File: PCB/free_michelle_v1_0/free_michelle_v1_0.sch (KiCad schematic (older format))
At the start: 28 parts

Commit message: Poprawione zapomniane polaczenie led WS do uC
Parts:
- removed J?: WS2812b, symbol Connector:Conn_01x03_Male
- added J?: WS2812b, symbol Connector:Conn_01x04_Male
- added J?: DS18B20, symbol Connector:Conn_01x04_Male
- U?: symbol free_michelle_v1_0-cache:grad73_library_24AA01 -> free_michelle_v1_0-rescue:grad73_library_24AA01-free_michelle_v1_0-cache
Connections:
- net labels added: DS18B20_1WIRE_PA15
- wire segments 203 -> 210
- no-connect marks 6 -> 8
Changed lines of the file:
@@
 $EndComp
 $Comp
-L free_michelle_v1_0-cache:grad73_library_24AA01 U?
+L free_michelle_v1_0-rescue:grad73_library_24AA01-free_michelle_v1_0-cache U?
 U 1 1 61E51F54
 P 2140 7830
@@
 NoConn ~ 9300 6090
 NoConn ~ 9300 6190
-$Comp
-L Connector:Conn_01x03_Male J?
-U 1 1 61FEF438
-P 12700 6000
-F 0 "J?" H 12808 6281 50  0000 C CNN
-F 1 "WS2812b" H 12808 6190 50  0000 C CNN
-F 2 "" H 12700 6000 50  0001 C CNN
-F 3 "~" H 12700 6000 50  0001 C CNN
-	1    12700 6000
-	-1   0    0    1
-$EndComp
 $Comp
 L power:+5VP #PWR?
@@
 Wire Wire Line
 	11900 5600 11900 6000
+$Comp
+L Connector:Conn_01x04_Male J?
+U 1 1 622B6E8C
+P 12700 6100
+F 0 "J?" H 12672 5982 50  0000 R CNN
+F 1 "WS2812b" H 12672 6073 50  0000 R CNN
+F 2 "" H 12700 6100 50  0001 C CNN
+F 3 "~" H 12700 6100 50  0001 C CNN
+	1    12700 6100
+	-1   0    0    1
+$EndComp
+NoConn ~ 12500 6200
+$Comp
+L Connector:Conn_01x04_Male J?
+U 1 1 622CF0D8
+P 14660 6100
+F 0 "J?" H 14632 5982 50  0000 R CNN
+F 1 "DS18B20" H 14632 6073 50  0000 R CNN
+F 2 "" H 14660 6100 50  0001 C CNN
+F 3 "~" H 14660 6100 50  0001 C CNN
+	1    14660 6100
+	-1   0    0    1
+$EndComp
+$Comp
+L power:+5V #PWR?
+U 1 1 622CFE05
+P 14300 5800
+F 0 "#PWR?" H 14300 5650 50  0001 C CNN
+F 1 "+5V" H 14315 5973 50  0000 C CNN
+F 2 "" H 14300 5800 50  0001 C CNN
+F 3 "" H 14300 5800 50  0001 C CNN
+	1    14300 5800
+	1    0    0    -1
+$EndComp
+Wire Wire Line
+	14460 5900 14300 5900
+Wire Wire Line
+	14300 5900 14300 5800
+$Comp
+L power:GND #PWR?
+U 1 1 622DBDAF
+P 14300 6300
+F 0 "#PWR?" H 14300 6050 50  0001 C CNN
+F 1 "GND" H 14305 6127 50  0000 C CNN
+F 2 "" H 14300 6300 50  0001 C CNN
+F 3 "" H 14300 6300 50  0001 C CNN
+	1    14300 6300
+	1    0    0    -1
+$EndComp
+Wire Wire Line
+	14300 6300 14300 6100
+Wire Wire Line
+	14300 6100 14460 6100
+Text GLabel 14100 6000 0    39   Input ~ 0
+DS18B20_1WIRE_PA15
+Wire Wire Line
+	14460 6000 14100 6000
+NoConn ~ 14460 6200
+Wire Wire Line
+	9340 2260 8600 2260
+Text GLabel 8600 2260 0    39   Input ~ 0
+WS2812b_PA9
+Text GLabel 8590 2660 0    39   Input ~ 0
+DS18B20_1WIRE_PA15
+Wire Wire Line
+	8590 2660 9340 2660
 $EndSCHEMATC

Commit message: Dodane przekazniki z tranzystorami kluczującymi
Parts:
- added D? (x8): 1N4148, symbol Device:D_Small_ALT
- added J? (x8): ARK, symbol Connector:Conn_01x03_Female
- added K? (x8): FINDER-36.11, Relay_THT:Relay_SPDT_Finder_36.11, symbol Relay:FINDER-36.11
- added Q? (x8): MMBT4403_PNP, Package_TO_SOT_SMD:SOT-23, symbol Transistor_BJT:MMBT3906
- added R? (x8): 2.2k, symbol Device:R_Small
- added R? (x8): 10k, symbol Device:R_Small
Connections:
- net +3V3: now also Q?.2 (E), Q?.2 (E), Q?.2 (E), Q?.2 (E), Q?.2 (E), Q?.2 (E), Q?.2 (E), Q?.2 (E)
- net GND: now also R?.1, R?.1, R?.1, R?.1, R?.1, R?.1, R?.1, R?.1
- net RELAY4_PB12: now reaches GPIO_CONTROLLER.21 (PB12)
- net RELAY4_PB12: now also R?.1
- net RELAY3_PB13: now reaches GPIO_CONTROLLER.22 (PB13)
- net RELAY3_PB13: now also R?.1
- net RELAY2_PB14: now reaches GPIO_CONTROLLER.23 (PB14)
- net RELAY2_PB14: now also R?.1
- net RELAY1_PB15: now reaches GPIO_CONTROLLER.24 (PB15)
- net RELAY1_PB15: now also R?.1
- net LIGHT4_PB4: now reaches GPIO_CONTROLLER.32 (PB4)
- net LIGHT4_PB4: now also R?.1
- net LIGHT3_PB5: now reaches GPIO_CONTROLLER.33 (PB5)
- net LIGHT3_PB5: now also R?.1
- net LIGHT2_PB6: now reaches GPIO_CONTROLLER.34 (PB6)
- net LIGHT2_PB6: now also R?.1
- net LIGHT1_PB7: now reaches GPIO_CONTROLLER.35 (PB7)
- net LIGHT1_PB7: now also R?.1
- new net: Q?.1 (B), R?.2 (x8)
- new net: D?.1 (K), K?.A1, Q?.3 (C) (x8)
- new net: J?.2 (Pin_2), K?.11 (x8)
- new net: J?.1 (Pin_1), K?.12 (x8)
- new net: J?.3 (Pin_3), K?.14 (x8)
- new net: D?.2 (A), K?.A2, R?.2 (x8)
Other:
- moved on the sheet: C1, C?, CR2032, D?, J?, Q?, R1, R2, R3, R4, R5, R?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

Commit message: Dodao i podlaczona nRF24
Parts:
- added C?: 1uF, symbol Device:C_Small
- added U?: ESP-12E, RF_Module:ESP-12E, symbol RF_Module:ESP-12E
- added U?: NRF24L01_Breakout, RF_Module:nRF24L01_Breakout, symbol RF:NRF24L01_Breakout
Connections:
- net labels added: nRF24_CE_PB1, nRF24_CSN_PA11, nRF24_IRQ_PB2, nRF24_MISO_PA12, nRF24_MOSI_PA10, nRF24_SCK_PB0
- wire segments 418 -> 440
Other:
- moved on the sheet: R4, R5, U?

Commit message: Dodane opisy i podział bloków na schemacie
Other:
- note added: "MIKROKONTROLER DO STEROWANIA GPIO I CZUJNIKAMI"
- note added: "MIKROKONTROLER DO STEROWANIA MENU I TFT"
- note added: "PRZEKAŹNIKI"
- note added: "ZASILANIE"
- note added: "ŁĄCZNOŚĆ BEZPRZEWODOWA"
- moved on the sheet: C1, C?, CR2032, D?, GPIO_CONTROLLER, J?, K?, Q?, R1, R2, R3, R4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

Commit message: Dosane ESP do schematu
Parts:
- removed U?: ESP-12E, RF_Module:ESP-12E, symbol RF_Module:ESP-12E
- added J?: Zworka_RX, symbol Connector:Conn_01x02_Male
- added J?: Zworka_TX, symbol Connector:Conn_01x02_Male
- added U?: ESP8266_NodeMCU_v2, symbol grad73_library:ESP8266_NodeMCU_v2
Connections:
- net labels added: DS3231_SCL_I2C3_PA8, DS3231_SDA_I2C3_PB8, ESP_RX_TX_STM__U1_PA15, ESP_TX_RX_STM__U1_PB7
- wire segments 440 -> 455
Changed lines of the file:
@@
 NoConn ~ 5830 6500
 Text GLabel 4490 6500 0    39   Input ~ 0
-DS3231_SCL_PB6
+DS3231_SCL_I2C3_PA8
 Text GLabel 2840 3360 0    39   Input ~ 0
 DS3231_SCL_PB6
@@
 	2840 3360 2990 3360
 Text GLabel 4490 6600 0    39   Input ~ 0
-DS3231_SDA_PB7
+DS3231_SDA_I2C3_PB8
 Text GLabel 2840 3460 0    39   Input ~ 0
 DS3231_SDA_PB7
@@
 Wire Wire Line
 	9780 3320 10580 3320
-$Comp
-L RF_Module:ESP-12E U?
-U 1 1 6282E130
-P 2970 11730
-F 0 "U?" H 2970 12711 50  0000 C CNN
-F 1 "ESP-12E" H 2970 12620 50  0000 C CNN
-F 2 "RF_Module:ESP-12E" H 2970 11730 50  0001 C CNN
-F 3 "http://wiki.ai-thinker.com/_media/esp8266/esp8266_series_modules_user_manual_v1.1.pdf" H 2620 11830 50  0001 C CNN
-	1    2970 11730
-	1    0    0    -1
-$EndComp
-$Comp
-L power:GND #PWR?
-U 1 1 62831A59
-P 2970 12590
-F 0 "#PWR?" H 2970 12340 50  0001 C CNN
-F 1 "GND" H 2975 12417 50  0000 C CNN
-F 2 "" H 2970 12590 50  0001 C CNN
-F 3 "" H 2970 12590 50  0001 C CNN
-	1    2970 12590
-	1    0    0    -1
-$EndComp
-Wire Wire Line
-	2970 12590 2970 12430
-$Comp
-L power:+3.3V #PWR?
-U 1 1 6285E1BD
-P 2970 10650
-F 0 "#PWR?" H 2970 10500 50  0001 C CNN
-F 1 "+3.3V" H 2985 10823 50  0000 C CNN
-F 2 "" H 2970 10650 50  0001 C CNN
-F 3 "" H 2970 10650 50  0001 C CNN
-	1    2970 10650
-	1    0    0    -1
-$EndComp
-Wire Wire Line
-	2970 10930 2970 10650
 $Comp
 L RF:NRF24L01_Breakout U?
@@
 Text Notes 18490 1270 0    118  ~ 0
 ZASILANIE
+$Comp
+L grad73_library:ESP8266_NodeMCU_v2 U?
+U 1 1 6342D07E
+P 2860 10460
+F 0 "U?" H 2860 10528 118 0000 C CNN
+F 1 "ESP8266_NodeMCU_v2" H 2860 10335 118 0000 C CNN
+F 2 "" H 3210 10460 118 0001 C CNN
+F 3 "" H 3210 10460 118 0001 C CNN
+	1    2860 10460
+	1    0    0    -1
+$EndComp
+$Comp
+L Connector:Conn_01x02_Male J?
+U 1 1 634309E9
+P 3670 11760
+F 0 "J?" V 3732 11804 50  0000 L CNN
+F 1 "Zworka_RX" V 3823 11804 50  0000 L CNN
+F 2 "" H 3670 11760 50  0001 C CNN
+F 3 "~" H 3670 11760 50  0001 C CNN
+	1    3670 11760
+	0    1    1    0
+$EndComp
+Wire Wire Line
+	3570 11960 3410 11960
+$Comp
+L Connector:Conn_01x02_Male J?
+U 1 1 63464817
+P 3570 12260
+F 0 "J?" V 3724 12072 50  0000 R CNN
+F 1 "Zworka_TX" V 3633 12072 50  0000 R CNN
+F 2 "" H 3570 12260 50  0001 C CNN
+F 3 "~" H 3570 12260 50  0001 C CNN
+	1    3570 12260
+	0    -1   -1   0
+$EndComp
+Wire Wire Line
+	3570 12060 3410 12060
+$Comp
+L power:GND #PWR?
+U 1 1 634CC58F
+P 3470 12600
+F 0 "#PWR?" H 3470 12350 50  0001 C CNN
+F 1 "GND" H 3475 12427 50  0000 C CNN
+F 2 "" H 3470 12600 50  0001 C CNN
+F 3 "" H 3470 12600 50  0001 C CNN
+	1    3470 12600
+	1    0    0    -1
+$EndComp
+Wire Wire Line
+	3410 12160 3470 12160
+Wire Wire Line
+	3470 12160 3470 12510
+Wire Wire Line
+	2310 11760 2170 11760
+Wire Wire Line
+	2170 11760 2170 12160
+Wire Wire Line
+	2170 12510 3470 12510
+Wire Wire Line
+	3470 12510 3470 12600
+Connection ~ 3470 12510
+Wire Wire Line
+	2310 12160 2170 12160
+Connection ~ 2170 12160
+Wire Wire Line
+	2170 12160 2170 12510
+$Comp
+L power:+5V #PWR?
+U 1 1 63605998
+P 1870 12110
+F 0 "#PWR?" H 1870 11960 50  0001 C CNN
+F 1 "+5V" H 1885 12283 50  0000 C CNN
+F 2 "" H 1870 12110 50  0001 C CNN
+F 3 "" H 1870 12110 50  0001 C CNN
+	1    1870 12110
+	1    0    0    -1
+$EndComp
+Wire Wire Line
+	2310 12260 1870 12260
+Wire Wire Line
+	1870 12260 1870 12110
+Text GLabel 4280 11960 2    39   Input ~ 0
+ESP_RX_TX_STM__U1_PA15
+Wire Wire Line
+	3410 11460 4200 11460
+Wire Wire Line
+	4200 11460 4200 12510
+Wire Wire Line
+	4200 12510 3480 12510
+Wire Wire Line
+	4280 11960 3670 11960
+Text GLabel 4280 12060 2    39   Input ~ 0
+ESP_TX_RX_STM__U1_PB7
+Wire Wire Line
+	3670 12060 4280 12060
 $EndSCHEMATC

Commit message: Dosane przelaczniki wlaczania zasilania i zlacza do schematu
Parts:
- added C?: 47uF, symbol Device:CP_Small
- added C? (x2): 100nF, symbol Device:C_Small
- added D?: GREEN_USER_LED, symbol Device:LED
- added D?: RED_LED, symbol Device:LED
- added D?: YELLOW_LED, symbol Device:LED
- added J?: A02YYUW_GroveCON, symbol Connector:Conn_01x04_Male
- added J?: Gniazdo 9V DC 5,5x2,5, symbol Connector:Conn_01x02_Male
- added J?: Gniazdo 5VP DC 5,5x2,5, symbol Connector:Conn_01x02_Male
- added R?: 110, symbol Device:R_Small
- added R?: 730, symbol Device:R_Small
- added R?: 290, symbol Device:R_Small
- added SW?: Rotary_Encoder_Switch, symbol Device:Rotary_Encoder_Switch
- added SW? (x2): SW_Push, symbol Switch:SW_Push
- added U?: LD1117V33, symbol grad73_library:LD1117V33
- J? (x2): value SW -> GROVE_SW
- J?: value WS2812b -> WS2812b_GroveCON
- J?: value DS18B20 -> DS18B20_GroveCON
- U?: value DS3231M -> DS3231M_RTC
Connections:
- net DS3231_SCL_I2C3_PA8 is gone; now on net DS3231_SCL_PB6: R2.1, R3.1, U?.16 (SCL)
- net DS3231_SDA_I2C3_PB8 is gone; now on net DS3231_SDA_PB9: U?.15 (SDA)
- net DS3231_SDA_PB7 is gone; now on net ESP_TX_RX_STM__U1_PB7: TFT_CONTROLLER.35 (PB7)
- net +3V3: no longer Q?.2 (E), Q?.2 (E), Q?.2 (E), Q?.2 (E), Q?.2 (E), Q?.2 (E), Q?.2 (E), Q?.2 (E)
- net +5V: now also J?.2 (Pin_2), J?.4 (Pin_4), SW?.A
- net +5VP: now also R?.1
- net +9V: now also C?.1, C?.1, R?.1, U?.1 (IN)
- net ESP_RX_TX_STM__U1_PA15: now also TFT_CONTROLLER.30 (PA15)
- net ESP_TX_RX_STM__U1_PB7: no longer J?.2 (Pin_2)
- net GND: now also C?.2, C?.2, C?.2, J?.1 (Pin_1), J?.1 (Pin_1), J?.3 (Pin_3), R?.1, SW?.B, U?.2 (GND)
- net DS3231_SDA_PB9: now reaches TFT_CONTROLLER.37 (PB9)
- net ENC_DT_PA0: now reaches TFT_CONTROLLER.6 (PA0)
- net ENC_DT_PA0: now also SW?.S1
- net ENC_CLK_PA1: now reaches TFT_CONTROLLER.7 (PA1)
- net ENC_CLK_PA1: now also SW?.S2
- net USER_LED_PA10: now reaches GPIO_CONTROLLER.27 (PA10)
- net USER_LED_PA10: now also D?.2 (A)
- net A02YYUW_U6_RX_PA12: now reaches GPIO_CONTROLLER.29 (PA12)
- net A02YYUW_U6_RX_PA12: now also J?.1 (Pin_1)
- new net: D?.1 (K), R?.2 (x3)
- new net: J?.2 (Pin_2), SW?.2 (x2)
- new net: D?.2 (A), SW?.1 (x2)
- new net +3.3VP: C?.1, Q?.2 (E), Q?.2 (E), Q?.2 (E), Q?.2 (E), Q?.2 (E), Q?.2 (E), Q?.2 (E), Q?.2 (E), U?.3 (OUT)
- no-connect marks 8 -> 59
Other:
- note added: "NAPIĘCIE ZASILANIA 3,3V"
- note added: "NAPIĘCIE ZASILANIA 5V"
- moved on the sheet: C?, D?, J?, K?, Q?, R4, R5, R?, U?

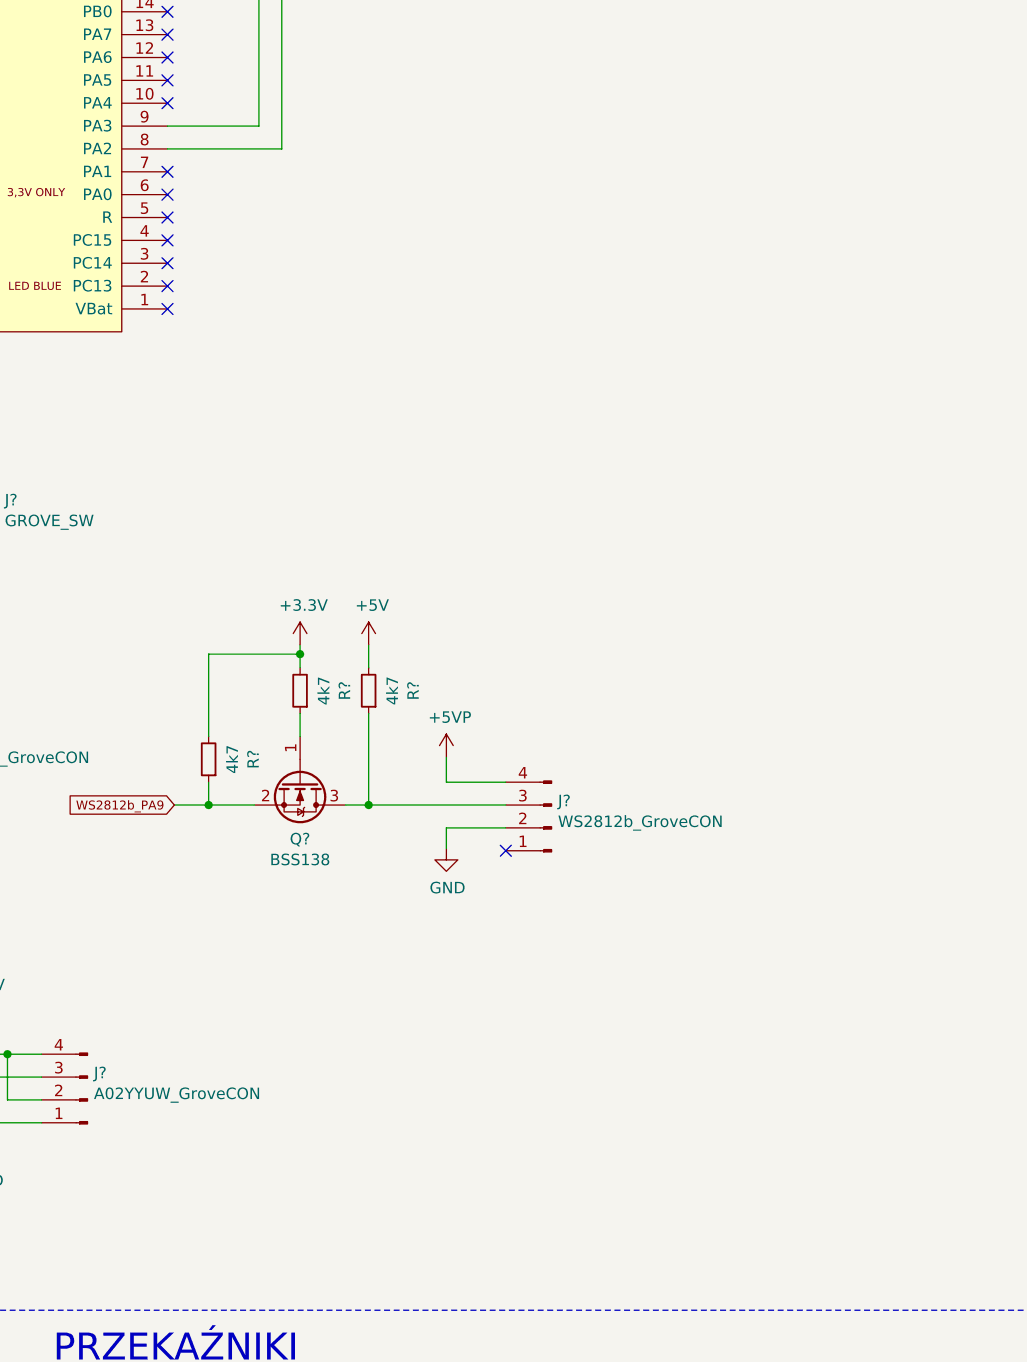
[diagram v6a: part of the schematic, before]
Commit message: Dodany Buzzer
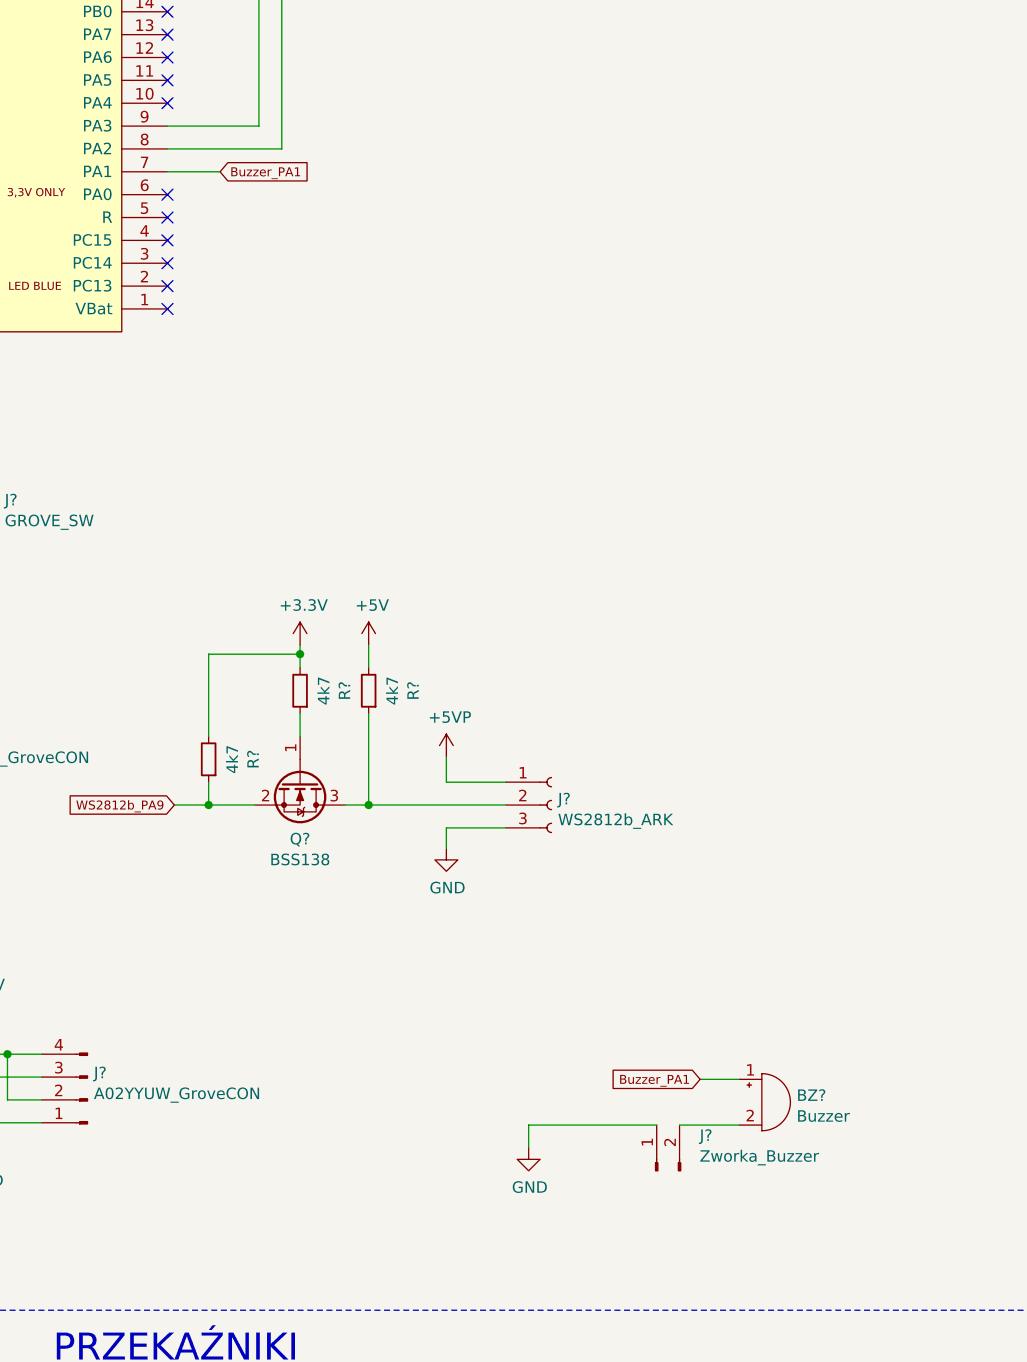
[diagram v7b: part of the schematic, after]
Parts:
- removed J?: WS2812b_GroveCON, symbol Connector:Conn_01x04_Male
- added BZ?: Buzzer, symbol Device:Buzzer
- added J?: WS2812b_ARK, symbol Connector:Conn_01x03_Female
- added J?: Zworka_Buzzer, symbol Connector:Conn_01x02_Male
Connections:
- net +5VP: now also J?.1 (Pin_1)
- net GND: now also J?.1 (Pin_1), J?.3 (Pin_3)
- net Buzzer_PA1: now reaches GPIO_CONTROLLER.7 (PA1)
- net Buzzer_PA1: now also BZ?.1 (-)
- net at Q?.3 (D), R?.1: now also J?.2 (Pin_2)
- new net: BZ?.2 (+), J?.2 (Pin_2)
- no-connect marks 59 -> 57
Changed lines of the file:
@@
-$Comp
-L Connector:Conn_01x04_Male J?
-U 1 1 622B6E8C
-P 14060 6390
-F 0 "J?" H 14032 6272 50  0000 R CNN
-F 1 "WS2812b_GroveCON" H 14032 6363 50  0000 R CNN
-F 2 "" H 14060 6390 50  0001 C CNN
-F 3 "~" H 14060 6390 50  0001 C CNN
-	1    14060 6390
-	-1   0    0    1
-$EndComp
-NoConn ~ 13860 6490
 $Comp
 L Connector:Conn_01x04_Male J?
@@
 NoConn ~ 12380 3120
 NoConn ~ 12380 3220
-NoConn ~ 12380 3520
 NoConn ~ 12380 3620
 NoConn ~ 12380 3720
@@
 	1    0    0    -1
 $EndComp
+$Comp
+L Connector:Conn_01x03_Female J?
+U 1 1 65A8E109
+P 14060 6290
+F 0 "J?" H 14088 6316 50  0000 L CNN
+F 1 "WS2812b_ARK" H 14088 6225 50  0000 L CNN
+F 2 "" H 14060 6290 50  0001 C CNN
+F 3 "~" H 14060 6290 50  0001 C CNN
+	1    14060 6290
+	1    0    0    -1
+$EndComp
+$Comp
+L Device:Buzzer BZ?
+U 1 1 65B5BEF5
+P 14980 7590
+F 0 "BZ?" H 15132 7619 50  0000 L CNN
+F 1 "Buzzer" H 15132 7528 50  0000 L CNN
+F 2 "" V 14955 7690 50  0001 C CNN
+F 3 "~" V 14955 7690 50  0001 C CNN
+	1    14980 7590
+	1    0    0    -1
+$EndComp
+$Comp
+L Connector:Conn_01x02_Male J?
+U 1 1 65B5C71B
+P 14520 7890
+F 0 "J?" V 14674 7702 50  0000 R CNN
+F 1 "Zworka_Buzzer" V 14583 7702 50  0000 R CNN
+F 2 "" H 14520 7890 50  0001 C CNN
+F 3 "~" H 14520 7890 50  0001 C CNN
+	1    14520 7890
+	0    -1   -1   0
+$EndComp
+Wire Wire Line
+	14620 7690 14880 7690
+$Comp
+L power:GND #PWR?
+U 1 1 65C2BC51
+P 13960 7790
+F 0 "#PWR?" H 13960 7540 50  0001 C CNN
+F 1 "GND" H 13965 7617 50  0000 C CNN
+F 2 "" H 13960 7790 50  0001 C CNN
+F 3 "" H 13960 7790 50  0001 C CNN
+	1    13960 7790
+	1    0    0    -1
+$EndComp
+Wire Wire Line
+	13960 7790 13960 7690
+Wire Wire Line
+	13960 7690 14520 7690
+Text GLabel 14710 7490 0    39   Input ~ 0
+Buzzer_PA1
+Wire Wire Line
+	14710 7490 14880 7490
+Text GLabel 12610 3520 2    39   Input ~ 0
+Buzzer_PA1
+Wire Wire Line
+	12380 3520 12610 3520
 $EndSCHEMATC

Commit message: Poprzypisywane footprinty do glownych urzadzen
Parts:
- removed R? (x8): 10k, symbol Device:R_Small
- removed SW?: Rotary_Encoder_Switch, symbol Device:Rotary_Encoder_Switch
- added C2, C3, C4, C6, C7, C8: 100nF, symbol Device:C_Small
- added R6, R7: 10k, symbol Device:R_Small
- added SW1: Rotary_Encoder, Rotary_Encoder:RotaryEncoder_Alps_EC12E_Vertical_H20mm, symbol Device:Rotary_Encoder
- BZ1: renamed from BZ?; footprint (none) -> Buzzer_Beeper:Buzzer_15x7.5RM7.6
- CR2032: footprint (none) -> grados73:CR2032_KOSZYK
- D11: renamed from D?; footprint (none) -> LED_THT:LED_D3.0mm_Clear
- D2: renamed from D?; footprint (none) -> LED_THT:LED_D3.0mm_IRGrey
- GPIO_CONTROLLER1: renamed from GPIO_CONTROLLER; footprint (none) -> grados73:grados73_BlackPill_STM32F4x1
- J1, J12, J2: renamed from J?; footprint (none) -> Connector_PinHeader_2.54mm:PinHeader_1x02_P2.54mm_Vertical
- J3, J8, J9: renamed from J?; footprint (none) -> Connector_PinHeader_2.00mm:PinHeader_1x04_P2.00mm_Horizontal
- LED1: renamed from J?; footprint (none) -> Connector_PinHeader_2.54mm:PinHeader_1x03_P2.54mm_Vertical
- SW2, SW3: renamed from SW?; footprint (none) -> grados73:Switch_BS800L
- TFT_CONTROLLER1: renamed from TFT_CONTROLLER; footprint (none) -> grados73:grados73_BlackPill_STM32F4x1
- Term1: renamed from J?; footprint (none) -> Connector_PinHeader_2.00mm:PinHeader_1x04_P2.00mm_Vertical
- U1: renamed from U?; footprint (none) -> Package_DIP:DIP-8_W7.62mm_LongPads
- U5: renamed from U?; footprint (none) -> Connector_PinHeader_2.54mm:PinHeader_1x06_P2.54mm_Horizontal
- U6, U7, U8: renamed from U?; footprint (none) -> Package_TO_SOT_THT:TO-220-3_Vertical
- gave numbers to parts that had none: 64
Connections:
- net +3V3: now also C2.1, C3.2, C4.2, C6.1, R6.1, R7.1
- net +5V: now also C7.1, C8.1
- net ENC_CLK_PA1: now also R7.2, SW1.B
- net ENC_DT_PA0: now also R6.2, SW1.A
- net GND: now also D10.2 (A), D3.2 (A), D4.2 (A), D5.2 (A), D6.2 (A), D7.2 (A), D8.2 (A), D9.2 (A), K1.A2, K2.A2, K3.A2, K4.A2, K5.A2, K6.A2, K7.A2, K8.A2, C2.2, C3.1, C4.1, C6.2, C7.2, C8.2, SW1.C
- no-connect marks 57 -> 56
